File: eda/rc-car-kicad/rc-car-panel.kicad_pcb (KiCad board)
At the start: 2 copper layers, 72 x 60 mm, 64 parts, among them J1 Servo Sig, J10 RF 3.3V, J11 RF CE, J12 RF CSN, J13 RF SCK, J14 RF MOSI, J15 RF MISO, J16 Gnd, J17 3.3V, J19 Battery, J2 Servo Gnd, J20 8.2V, J4 DC Motor -, J5 DC Motor +, J6 ISP RESET, J9 RF Gnd, Q1 IRLML6244, Q2 IRLML2246, Q3 IRLML2246, Q4 IRLML6244, Q5 MMBT3904, Q6 MMBT3904, SW1 SW_SPST, U1 TPS3840, U3 ATmega164A-A

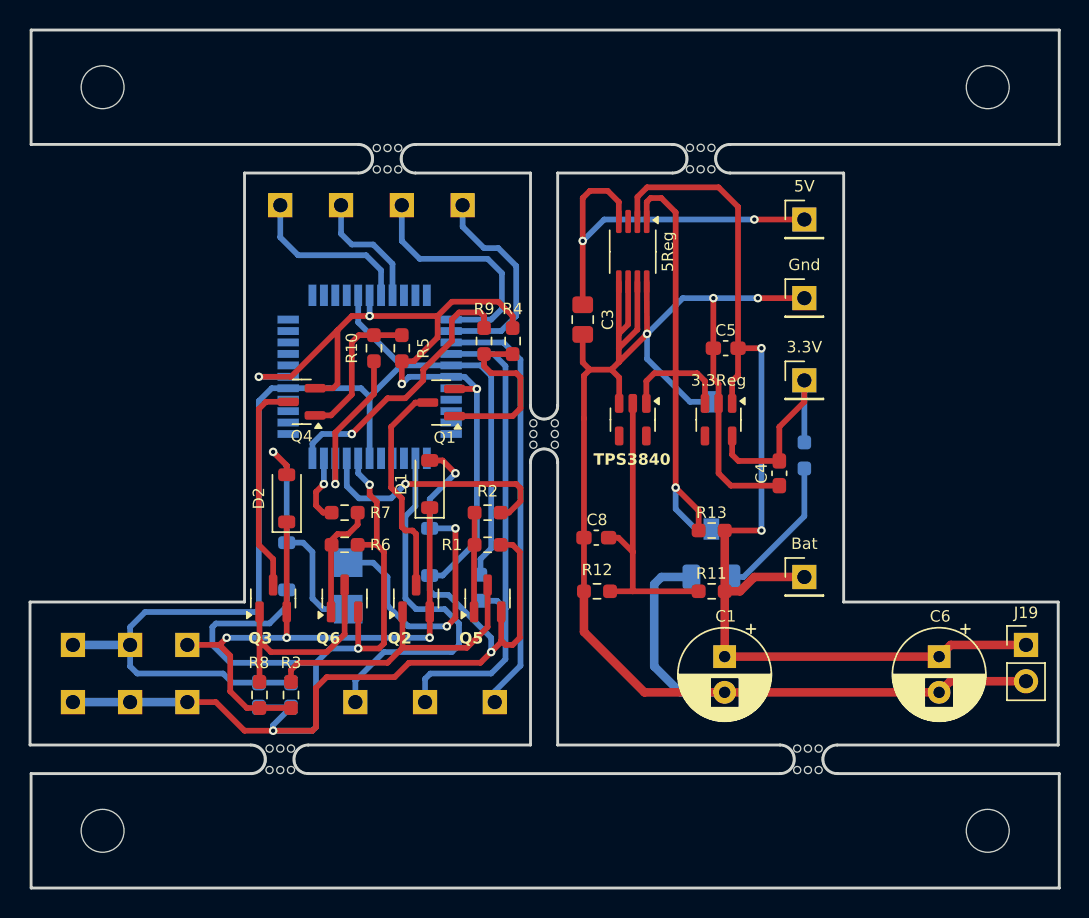
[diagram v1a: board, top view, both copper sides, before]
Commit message: - Updated panelized board. Fixed all design route errors
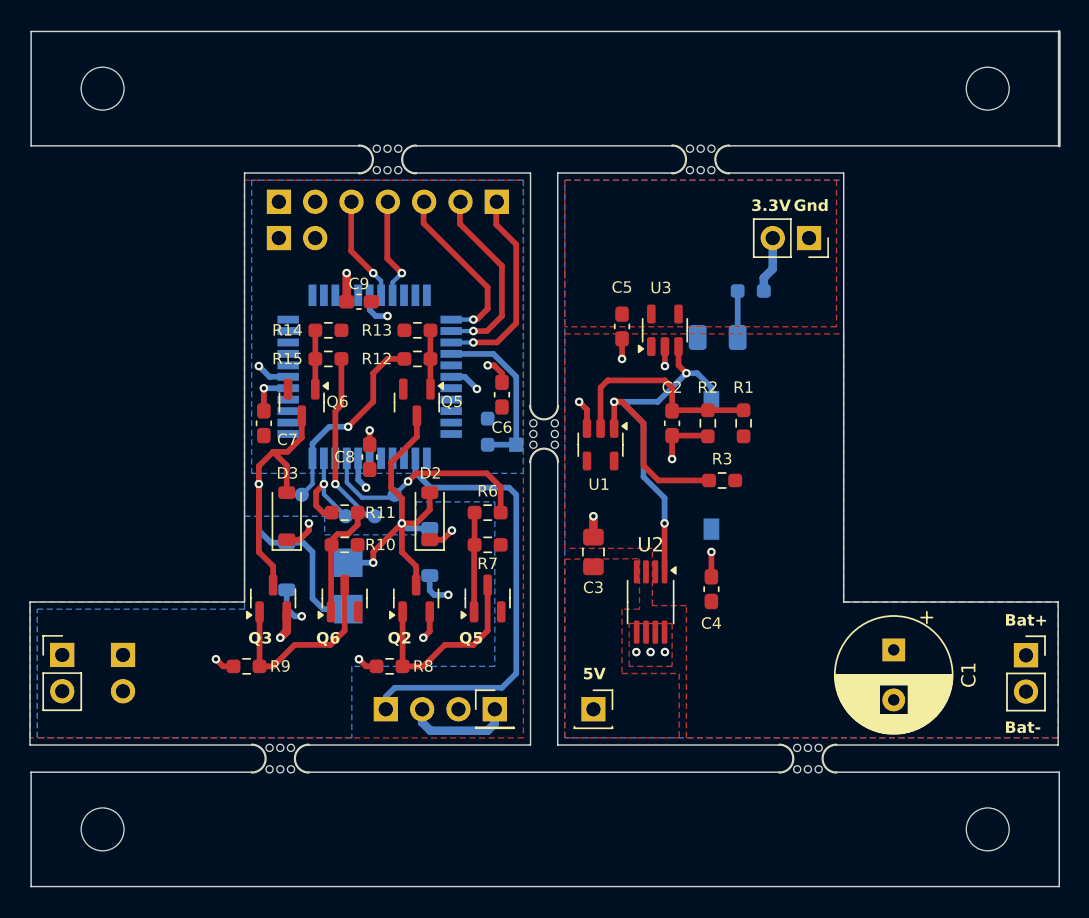
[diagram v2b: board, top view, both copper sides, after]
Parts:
- removed 3.3Reg: MIC5225-3.3YM5, Package_TO_SOT_SMD:SOT-23-5
- removed 3.3V: 3.3V, Connector_PinHeader_2.54mm:PinHeader_1x01_P2.54mm_Vertical
- removed 5Reg: MIC3975-5.0YMM, Package_SO:MSOP-8_3x3mm_P0.65mm
- removed 5V: Servo 5V, Connector_PinHeader_2.54mm:PinHeader_1x01_P2.54mm_Vertical
- removed Bat, J20: 8.2V, Connector_PinHeader_2.54mm:PinHeader_1x01_P2.54mm_Vertical
- removed Gnd: Gnd, Connector_PinHeader_2.54mm:PinHeader_1x01_P2.54mm_Vertical
- removed J19: Battery, Connector_PinHeader_2.54mm:PinHeader_1x02_P2.54mm_Vertical
- added C9: .1uF, Capacitor_SMD:C_0603_1608Metric_Pad1.08x0.95mm_HandSolder, F.Cu at (135.1, 85.5)
- added J3: ~, Connector_PinSocket_2.54mm:PinSocket_1x02_P2.54mm_Vertical, F.Cu at (166.5, 81.0)
- added J7: ~, _global-libraries:PinHeader_1x02_P2.54mm_Vertical_No_Courtyard, B.Cu at (129.5, 78.5)
- added J8: ~, Connector_PinHeader_2.54mm:PinHeader_1x05_P2.54mm_Vertical, B.Cu at (144.7, 78.5)
- added U2: MIC3975-5.0YMM, Package_SO:MSOP-8_3x3mm_P0.65mm, F.Cu at (155.4, 106.5)
- added U4: ATmega164A-A, Package_QFP:TQFP-44_10x10mm_P0.8mm, B.Cu at (135.8, 90.8)
- C1: value 100uF -> 200uF; footprint Capacitor_THT:CP_Radial_D6.3mm_P2.50mm -> Capacitor_THT:CP_Radial_D8.0mm_P3.50mm
- C2: value .1uF -> 1uF; moved to F.Cu
- C4: value 2.2uF -> 1uF
- C5: value 1uF -> 2.2uF
- C6: value 100uF -> .1uF; footprint Capacitor_THT:CP_Radial_D6.3mm_P2.50mm -> Capacitor_SMD:C_0603_1608Metric_Pad1.08x0.95mm_HandSolder
- C7, D3, R14: moved to F.Cu
- C8: value 1uF -> .1uF
- D1: value 1N5819HW-7-F -> LED; footprint Diode_SMD:D_SOD-123 -> LED_SMD:LED_1206_3216Metric; moved to B.Cu
- D5: value LED -> 1N5819HW-7-F; footprint LED_SMD:LED_1206_3216Metric -> Diode_SMD:D_SOD-123
- J1: value Servo Sig -> ~; footprint Connector_PinHeader_2.54mm:PinHeader_1x01_P2.54mm_Vertical -> Connector_PinSocket_2.54mm:PinSocket_1x02_P2.54mm_Vertical; moved to F.Cu
- J10: value RF 3.3V -> ~; footprint Connector_PinHeader_2.54mm:PinHeader_1x01_P2.54mm_Vertical -> TestPoint:TestPoint_Pad_2.0x2.0mm
- J11: value RF CE -> ~; footprint Connector_PinHeader_2.54mm:PinHeader_1x01_P2.54mm_Vertical -> TestPoint:TestPoint_Pad_1.0x1.0mm
- J12: value RF CSN -> ~; footprint Connector_PinHeader_2.54mm:PinHeader_1x01_P2.54mm_Vertical -> TestPoint:TestPoint_Pad_D1.0mm
- J13: value RF SCK -> ~; footprint Connector_PinHeader_2.54mm:PinHeader_1x01_P2.54mm_Vertical -> TestPoint:TestPoint_Pad_D1.0mm
- J14: value RF MOSI -> ~; footprint Connector_PinHeader_2.54mm:PinHeader_1x01_P2.54mm_Vertical -> TestPoint:TestPoint_Pad_D1.0mm
- J15: value RF MISO -> ~; footprint Connector_PinHeader_2.54mm:PinHeader_1x01_P2.54mm_Vertical -> TestPoint:TestPoint_Pad_D1.0mm
- J16: value Gnd -> ~; footprint Connector_PinHeader_2.54mm:PinHeader_1x01_P2.54mm_Vertical -> _global-libraries:PinHeader_1x02_P2.54mm_Vertical_No_Courtyard; moved to F.Cu
- J17: value 3.3V -> ~; moved to F.Cu
- J2: value Servo Gnd -> ~; footprint Connector_PinHeader_2.54mm:PinHeader_1x01_P2.54mm_Vertical -> Connector_PinSocket_2.54mm:PinSocket_1x01_P2.54mm_Vertical; moved to F.Cu
- J4: value DC Motor - -> ~; footprint TestPoint:TestPoint_Pad_2.0x2.0mm -> Connector_PinHeader_2.54mm:PinHeader_1x02_P2.54mm_Vertical; moved to F.Cu
- J5: value DC Motor + -> ~; footprint TestPoint:TestPoint_Pad_2.0x2.0mm -> Connector_PinHeader_2.54mm:PinHeader_1x02_P2.54mm_Vertical
- J6: value ISP RESET -> ~; footprint Connector_PinHeader_2.54mm:PinHeader_1x01_P2.54mm_Vertical -> Connector_PinHeader_2.54mm:PinHeader_1x03_P2.54mm_Vertical
- J9: value RF Gnd -> ~; footprint Connector_PinHeader_2.54mm:PinHeader_1x01_P2.54mm_Vertical -> TestPoint:TestPoint_Pad_2.0x2.0mm
- Q1, Q4: value IRLML6244 -> MMBT3904
- Q5, Q6: value MMBT3904 -> IRLML6244
- R1: value 1.3k -> 470k
- R10: value 10 -> 1.3k
- R11: value 953k -> 1.3k
- R12: value 1M -> 10
- R13: value 150k -> 10k
- R15: value 1.5k -> 10; moved to F.Cu
- R2: value 1.3k -> 500k
- R3: value 10k -> 150k
- R4: value 10k -> 1.5k; moved to B.Cu
- R5: moved to B.Cu
- R9: value 10 -> 10k
- U3: value ATmega164A-A -> MIC5225-3.3YM5; footprint Package_QFP:TQFP-44_10x10mm_P0.8mm -> Package_TO_SOT_SMD:SOT-23-5; moved to F.Cu
- moved J1 47.0 mm to (181.7, 110.2), turned to 0 degrees
- moved C6 35.6 mm to (145.1, 92.0)
- moved J16 35.5 mm to (129.5, 81.0), turned to 90 degrees
- moved R15 34.0 mm to (132.9, 89.5), turned to 0 degrees
- moved R3 33.7 mm to (160.4, 98.0), turned to 180 degrees
- moved C2 32.7 mm to (156.9, 94.0)
- moved J17 29.8 mm to (144.6, 114.0), turned to 0 degrees
- moved D5 29.7 mm to (130.0, 104.0), turned to -90 degrees
- moved J2 28.4 mm to (151.4, 114.0), turned to 0 degrees
- moved R9 28.2 mm to (127.2, 111.0), turned to 0 degrees
- moved R11 26.3 mm to (134.1, 100.2)
- moved R13 24.9 mm to (139.1, 87.5)
- moved J11 23.5 mm to (146.1, 95.5)
- moved J15 23.2 mm to (131.1, 99.0)
- moved D1 22.6 mm to (160.1, 88.0), turned to 0 degrees
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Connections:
- C2 pad 1: +3.3V -> /U1-VDD
- C2 pad 2: GND -> GND Main
- C3 pad 1: +5V -> +5V Main
- C4 pad 1: +3.3V Main -> +8.2V Main
- C5 pad 1: +8.2V Main -> +3.3V Main
- C6 pad 1: +8.2V Main -> +3.3V
- C6 pad 2: GND Main -> GND
- C8 pad 1: Net-(U1-VDD) -> +3.3V
- C8 pad 2: GND Main -> GND
- D1 pad 1: +8.2V -> GND Main
- D3 pad 1: Net-(D2-A) -> +8.2V
- D3 pad 2: GND -> Net-(D3-A)
- D4 pad 1: Net-(D1-A) -> Net-(D2-A)
- D5 pad 1: GND Main -> Net-(D3-A)
- D5 pad 2: Net-(D5-A) -> GND
- J1 pad 1: /Servo Sig -> +8.2V Main
- J10 pad 1: +3.3V -> Net-(D3-A)
- J11 pad 1: /CE -> /RESET
- J12 pad 1: /CSN -> /Forward_Latch
- J13 pad 1: /SCK -> /Forward_PWM
- J14 pad 1: /MOSI -> /Reverse_Latch
- J15 pad 1: /MISO -> /Reverse_PWM
- J17 pad 1: +3.3V -> /Servo 5V
- J2 pad 1: GND -> +5V Main
- J4 pad 1: Net-(D2-A) -> +8.2V
- J5 pad 1: Net-(D1-A) -> +8.2V
- J6 pad 1: /RESET -> /Servo Sig
- J9 pad 1: GND -> Net-(D2-A)
- Q1 pad 1: Net-(Q1-G) -> Net-(Q1-B)
- Q1 pad 3: Net-(Q1-D) -> Net-(Q1-C)
- Q2 pad 1: Net-(Q2-G) -> Net-(Q1-C)
- Q2 pad 3: Net-(Q1-D) -> Net-(D2-A)
- Q3 pad 3: Net-(Q3-D) -> Net-(D3-A)
- Q4 pad 1: Net-(Q4-G) -> Net-(Q4-B)
- Q4 pad 3: Net-(Q3-D) -> Net-(Q3-G)
- Q5 pad 1: Net-(Q5-B) -> Net-(Q5-G)
- Q5 pad 3: Net-(Q2-G) -> Net-(D2-A)
- Q6 pad 1: Net-(Q6-B) -> Net-(Q6-G)
- Q6 pad 3: Net-(Q3-G) -> Net-(D3-A)
- R1 pad 1: Net-(Q5-B) -> +8.2V Main
- R1 pad 2: GND -> /U1-VDD
- R10 pad 1: Net-(Q4-G) -> Net-(Q4-B)
- R10 pad 2: /Forward_PWM -> GND
- R11 pad 1: +8.2V Main -> Net-(Q4-B)
- R11 pad 2: Net-(U1-VDD) -> /Reverse_Latch
- R12 pad 1: Net-(U1-VDD) -> /Reverse_PWM
- R12 pad 2: GND Main -> Net-(Q5-G)
- R13 pad 1: +8.2V Main -> Net-(Q5-G)
- R13 pad 2: Net-(SW1-B) -> GND
- R14 pad 1: +3.3V -> Net-(Q6-G)
- R14 pad 2: /RESET -> GND
- R15 pad 1: +3.3V Main -> Net-(Q6-G)
- R15 pad 2: Net-(D5-A) -> /Forward_PWM
- R2 pad 1: /Forward_Latch -> /U1-VDD
- R2 pad 2: Net-(Q5-B) -> GND Main
- R3 pad 1: +8.2V -> +8.2V Main
- R3 pad 2: Net-(Q2-G) -> /U1-Reset
- R4 pad 1: Net-(Q1-G) -> Net-(D1-A)
- R4 pad 2: GND -> +3.3V Main
- R5 pad 1: Net-(Q4-G) -> +3.3V
- R5 pad 2: GND -> /RESET
- R6 pad 1: Net-(Q6-B) -> /Forward_Latch
- R6 pad 2: GND -> Net-(Q1-B)
- R7 pad 1: Net-(Q6-B) -> Net-(Q1-B)
- R7 pad 2: /Reverse_Latch -> GND
- R8 pad 2: Net-(Q3-G) -> Net-(Q1-C)
- R9 pad 1: /Reverse_PWM -> +8.2V
- R9 pad 2: Net-(Q1-G) -> Net-(Q3-G)
- SW1 pad 2: Net-(SW1-B) -> /U1-Reset
- U1 pad 1: Net-(SW1-B) -> /U1-Reset
- U1 pad 2: Net-(U1-VDD) -> /U1-VDD
- U3 pad 1: /MOSI -> +8.2V Main
- U3 pad 2: /MISO -> GND Main
- U3 pad 3: /SCK -> /U1-Reset
- U3 pad 4: /RESET -> unconnected-(U3-BP-Pad4)
- U3 pad 5: +3.3V -> +3.3V Main
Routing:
- net GND: track 163.5 -> 14.3 mm, vias 8 -> 6
- net GND Main: track 130.9 -> 12.1 mm, vias 3 -> 9
- net +3.3V: track 85.3 -> 8.15 mm, vias 0 -> 4
- net +8.2V Main: track 76.7 -> 0.00 mm, vias 2 -> 0
- net Net-(SW1-B): track 39.1 -> 0.00 mm, vias 1 -> 0
- net /U1-Reset: track 0.00 -> 37.3 mm, vias 0 -> 3
- net +8.2V: track 42.6 -> 11.0 mm, vias 3 -> 6
- net Net-(D3-A): track 0.00 -> 31.0 mm, vias 0 -> 1
- net +5V: track 28.0 -> 0.00 mm, vias 2 -> 0
- net /RESET: track 34.5 -> 12.0 mm
- net Net-(D1-A): track 25.6 -> 3.25 mm, vias 3 -> 0
- net Net-(U1-VDD): track 21.4 -> 0.00 mm
- net Net-(Q2-G): track 21.3 -> 0.00 mm
- net /SCK: track 30.0 -> 14.2 mm, vias 0 -> 1
- net Net-(Q1-D): track 15.3 -> 0.00 mm
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- added copper zone on B.Cu, net +3.3V
- added copper zone on F.Cu, net +3.3V Main
- added copper zone on F.Cu, net +5V Main
- added copper zone on B.Cu, net +8.2V
- added copper zone on F.Cu, net +8.2V Main
- added copper zone on F.Cu, net GND
- added copper zone on B.Cu, net GND Main
- added copper zone on F.Cu, net GND Main
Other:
- board size 72 x 60 mm -> 72 x 59.8 mm
- board text added: "5V"
- board text added: "Bat+"
- board text added: "Bat-"
- board text added: "U1"
- board text added: "U3"
- board text added: "V+"
- board text added: "V-"
- board text removed: "Bat"
- board text removed: "Reset"
- board text removed: "Servo SIG"
- board text removed: "TPS3840"

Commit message: - Added an images directory with images of the pcb and the schematic - Added a revision number to the pcb. - Finalized pcb and schematic
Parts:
- removed J10, J9: ~, TestPoint:TestPoint_Pad_2.0x2.0mm
- added M+1: ~, TestPoint:TestPoint_Pad_2.0x2.0mm, B.Cu at (136.0, 108.0)
- added M-1: ~, TestPoint:TestPoint_Pad_2.0x2.0mm, B.Cu at (133.0, 108.0)
- C1: footprint Capacitor_THT:CP_Radial_D8.0mm_P3.50mm -> Capacitor_THT:CP_Radial_D6.3mm_P2.50mm
- moved C1 0.47 mm to (172.4, 110.3)
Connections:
- net +8.2V renamed +8.4V
- net +8.2V Main renamed +8.4V Main
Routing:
- net Net-(D3-A): track 31.0 -> 26.7 mm, vias 1 -> 2
- net Net-(D2-A): track 24.3 -> 26.8 mm
- net /Forward_Latch: track 15.8 -> 18.0 mm
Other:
- board text added: "M+"
- board text added: "M-"
- board text added: "QB.Creates"
- board text added: "pcb-rc-car-A1"
